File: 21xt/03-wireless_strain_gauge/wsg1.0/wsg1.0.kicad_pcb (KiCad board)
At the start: 2 copper layers, 34 parts, among them J1 GenConn3, J2 GenConn1, J3 GenConn2, U1 ADS1120, U2 102010388

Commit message: First layout 'draft'
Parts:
- removed C1: 22uF, Capacitor_SMD:C_0603_1608Metric
- removed C2: 47uF, Capacitor_SMD:C_0603_1608Metric
- removed R1: 806k, Resistor_SMD:R_0805_2012Metric
- removed R2: 80.6k, Resistor_SMD:R_0603_1608Metric
- added 22u: 22uF, Capacitor_SMD:C_0603_1608Metric, F.Cu at (127.7, 102.7)
- added 47u: 47uF, Capacitor_SMD:C_0603_1608Metric, F.Cu at (125.1, 102.8)
- added 80.6k: 80.6k, Resistor_SMD:R_0603_1608Metric, F.Cu at (124.8, 110.0)
- added 806k: 806k, Resistor_SMD:R_0805_2012Metric, F.Cu at (122.8, 106.4)
- added C13: 0.1uF, Capacitor_SMD:C_0603_1608Metric, F.Cu at (118.3, 120.1)
- added C14: 100uF, Capacitor_SMD:C_0603_1608Metric, F.Cu at (119.9, 120.1)
- TVS1: footprint Diode_THT:D_DO-201AE_P15.24mm_Horizontal -> Diode_SMD:D_0402_1005Metric
- moved J3 58.5 mm to (133.8, 131.0), turned to -90 degrees
- moved R4 57.9 mm to (104.5, 114.3), turned to -90 degrees
- moved R8 57.7 mm to (128.8, 131.3), turned to 90 degrees
- moved J2 55.9 mm to (133.3, 118.6), turned to -90 degrees
- moved C11 55.3 mm to (121.6, 126.1)
- moved C12 54.4 mm to (121.6, 127.6)
- moved J1 53.7 mm to (133.2, 106.5), turned to -90 degrees
- moved R6 53.7 mm to (106.4, 115.5), turned to -90 degrees
- moved U2 53.4 mm to (104.3, 127.8), turned to 90 degrees
- moved R5 53.3 mm to (112.4, 115.5), turned to -90 degrees
- moved C3 52.5 mm to (100.0, 115.0), turned to 180 degrees
- moved C8 51.0 mm to (101.0, 106.6), turned to 90 degrees
- moved C4 48.9 mm to (100.0, 113.4), turned to 180 degrees
- moved R7 46.7 mm to (114.1, 114.1), turned to -90 degrees
- moved C9 44.5 mm to (105.5, 104.2), turned to 90 degrees
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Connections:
- DAC1 pad 2: CS -> CS-DAC
- DAC1 pad 6: DacClr -> unconnected-(DAC1-CLR#-Pad6)
- R7 pad 2: CS -> CS-ADC
- U2 pad 1: DacClr -> CS-DAC
- U2 pad 4: CS -> CS-ADC
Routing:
- net 3v3: track 0.00 -> 52.7 mm
- net CS-ADC: track 0.00 -> 28.8 mm, vias 0 -> 2
- net CS-DAC: track 0.00 -> 27.4 mm, vias 0 -> 1
- net DacLoad: track 0.00 -> 25.1 mm
- net GND: track 0.00 -> 24.3 mm, vias 0 -> 27
- net Ready: track 0.00 -> 22.8 mm
- net GND1: track 0.00 -> 20.4 mm, vias 0 -> 15
- net MOSI: track 0.00 -> 19.6 mm, vias 0 -> 1
- net SClk: track 0.00 -> 15.5 mm
- net Net-(U1-REFP0): track 0.00 -> 12.2 mm
- net 5.5V: track 0.00 -> 11.6 mm, vias 0 -> 10
- net Net-(BConv1-VIN): track 0.00 -> 11.5 mm
- net Net-(LinReg1-VOUT): track 0.00 -> 11.3 mm
- net Net-(InstrAmp1--IN): track 0.00 -> 9.66 mm
- net Net-(InstrAmp1-+IN): track 0.00 -> 9.46 mm
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- added copper zone on In1.Cu, net 5.5V
- added copper zone on F.Cu, net GND
- added copper zone on B.Cu, net GND1
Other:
- board outline added: 47.6 x 40 mm
- copper layers 2 -> 4
- board text added: "0.1u"
- board text added: "100u"
- board text added: "5u"

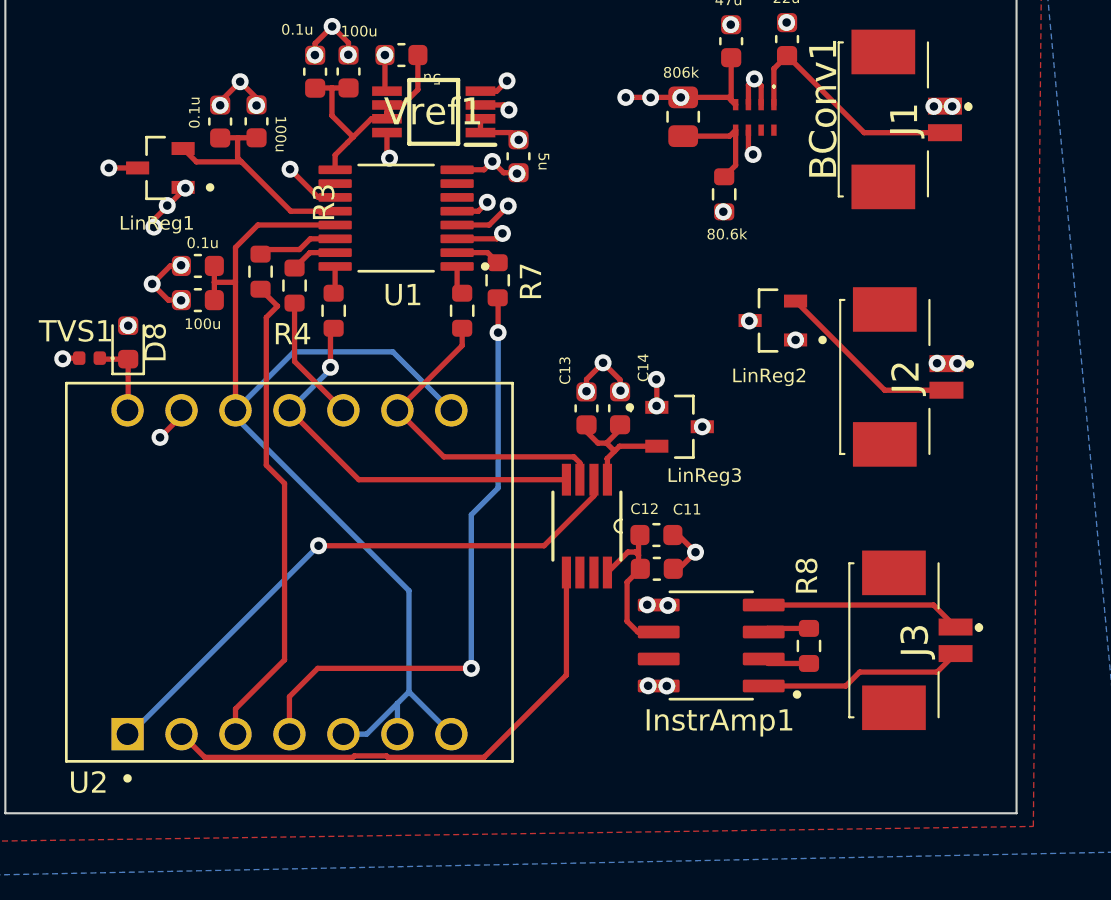
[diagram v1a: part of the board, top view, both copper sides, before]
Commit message: fixed some mistakes in previous layout
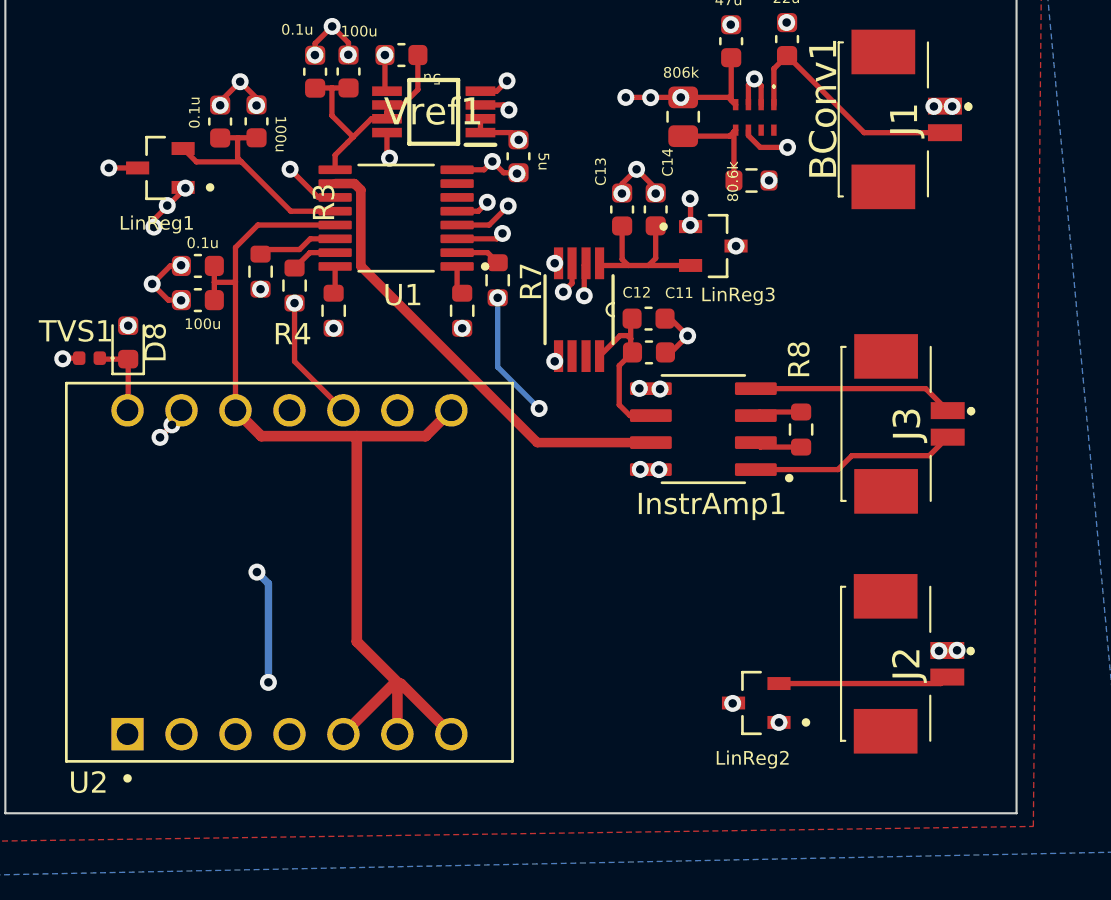
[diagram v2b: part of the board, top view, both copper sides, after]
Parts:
- moved LinReg2 18.0 mm to (126.3, 134.0)
- moved J2 13.5 mm to (133.4, 132.1)
- moved C11 10.2 mm to (121.2, 115.9)
- moved C12 10.2 mm to (121.2, 117.5)
- moved DAC1 10.2 mm to (117.9, 115.5)
- moved InstrAmp1 10.2 mm to (123.8, 121.1)
- moved R8 10.2 mm to (128.4, 121.1)
- moved J3 10.2 mm to (133.4, 120.8)
- moved C13 9.51 mm to (120.0, 110.7)
- moved C14 9.51 mm to (121.5, 110.7)
- moved LinReg3 8.65 mm to (124.2, 112.5)
- moved 80.6k 1.44 mm to (126.0, 109.4), turned to 0 degrees
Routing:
- net AmplifiedSig: track 0.00 -> 22.0 mm
- net MISO: track 6.00 -> 16.7 mm, vias 0 -> 1
- net CS-DAC: track 27.4 -> 32.1 mm
- net 3v3: track 52.7 -> 48.8 mm
- net CS-ADC: track 28.8 -> 26.2 mm
- net Net-(DAC1-VDD): track 6.74 -> 8.31 mm
- net SClk: track 15.5 -> 16.8 mm, vias 0 -> 2
- net GND: track 24.3 -> 25.4 mm
- net MOSI: track 19.6 -> 20.6 mm, vias 1 -> 2
- net Ready: track 22.8 -> 23.7 mm, vias 0 -> 3
- net Net-(J2-Pin_2): track 8.84 -> 8.05 mm
- net GND1: track 20.4 -> 20.0 mm, vias 15 -> 16
- net DacLoad: track 25.1 -> 24.8 mm, vias 0 -> 1

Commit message: hi
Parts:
- added REF**: MountingHole_2.1mm, MountingHole:MountingHole_2.1mm, F.Cu at (145.4, 141.8)
- added REF**: MountingHole_2.1mm, MountingHole:MountingHole_2.1mm, F.Cu at (85.7, 97.5)
- added REF**: MountingHole_2.1mm, MountingHole:MountingHole_2.1mm, F.Cu at (85.0, 141.8)
- added REF**: MountingHole_2.1mm, MountingHole:MountingHole_2.1mm, F.Cu at (144.8, 98.2)
- TVS1: footprint Diode_SMD:D_0402_1005Metric -> Diode_SMD:D_0603_1608Metric
- moved TVS1 0.87 mm to (94.0, 117.8)
- renumbered 22u to C1, 47u to C2, 806k to R1, 80.6k to R2
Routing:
- net 5.5V: track 11.6 -> 13.9 mm, vias 10 -> 12
- net Net-(D8-K): track 3.78 -> 4.33 mm
- net GND: track 25.4 -> 25.9 mm, vias 27 -> 28
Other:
- board size 47.6 x 40 mm -> 67.1 x 51.4 mm

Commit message: hi
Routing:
- net GND: track 25.9 -> 24.7 mm, vias 28 -> 1
- net GND1: track 20.0 -> 20.8 mm

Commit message: hi reid
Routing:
- net GND: track 24.7 -> 29.9 mm, vias 1 -> 28
- net GND1: track 20.8 -> 21.4 mm, vias 16 -> 19

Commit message: oopsie
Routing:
- added copper zone on In2.Cu, net 5.5V
- added copper zone on B.Cu, net GND
- added copper zone on In1.Cu, net GND1
- removed copper zone on In1.Cu, net 5.5V
- removed copper zone on B.Cu, net GND1
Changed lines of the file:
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@@
   (segment (start 116.05 120.1) (end 114.1 118.15) (width 0.25) (layer "B.Cu") (net 33))
   (segment (start 114.1 118.15) (end 114.1 114.89) (width 0.25) (layer "B.Cu") (net 33))
-  (zone (net 2) (net_name "GND") (layer "F.Cu") (hatch edge 0.5)
+  (zone (net 2) (net_name "GND") (layers "F&B.Cu") (hatch edge 0.5)
+    (priority 2)
+    (connect_pads (clearance 0.5))
+    (min_thickness 0.25) (filled_areas_thickness no)
+    (fill yes (thermal_gap 0.5) (thermal_bridge_width 0.5))
+    (polygon
+      (pts
+        (xy 153.88 88.43)
+        (xy 75.17 89.26)
+        (xy 78.32 150.7)
+        (xy 157.7 148.21)
+      )
+    )
+  )
+  (zone (net 8) (net_name "GND1") (layer "In1.Cu") (hatch edge 0.5)
+    (connect_pads (clearance 0.5))
+    (min_thickness 0.25) (filled_areas_thickness no)
+    (fill yes (thermal_gap 0.5) (thermal_bridge_width 0.5))
+    (polygon
+      (pts
+        (xy 79.08 91.14)
+        (xy 80.22 146.63)
+        (xy 151.86 146.14)
+        (xy 150.39 91.96)
+      )
+    )
+  )
+  (zone (net 3) (net_name "5.5V") (layer "In2.Cu") (hatch edge 0.5)
     (priority 1)
     (connect_pads (clearance 0.5))
@@
     (polygon
       (pts
-        (xy 163.66 92.24)
-        (xy 69.28 89.89)
-        (xy 76.57 146.84)
-        (xy 157.11 151.78)
+        (xy 152.02 90.49)
+        (xy 77.45 90.49)
+        (xy 79.73 148.42)
+        (xy 155.13 147.28)
       )
     )
-  )
-  (zone (net 3) (net_name "5.5V") (layer "In1.Cu") (hatch edge 0.5)
-    (connect_pads (clearance 0.5))
-    (min_thickness 0.25) (filled_areas_thickness no)
-    (fill yes (thermal_gap 0.5) (thermal_bridge_width 0.5))
-    (polygon
-      (pts
-        (xy 166.99 88.78)
-        (xy 64.96 86.31)
-        (xy 74.59 148.07)
-        (xy 163.41 155.73)
-      )
-    )
-  )
-  (zone (net 8) (net_name "GND1") (layer "B.Cu") (hatch edge 0.5)
-    (priority 2)
-    (connect_pads (clearance 0.5))
-    (min_thickness 0.25) (filled_areas_thickness no)
-    (fill yes (thermal_gap 0.5) (thermal_bridge_width 0.5))
-    (polygon
-      (pts
-        (xy 169.46 85.69)
-        (xy 62.11 84.45)
-        (xy 68.66 154.37)
-        (xy 165.38 158.57)
-      )
-    )

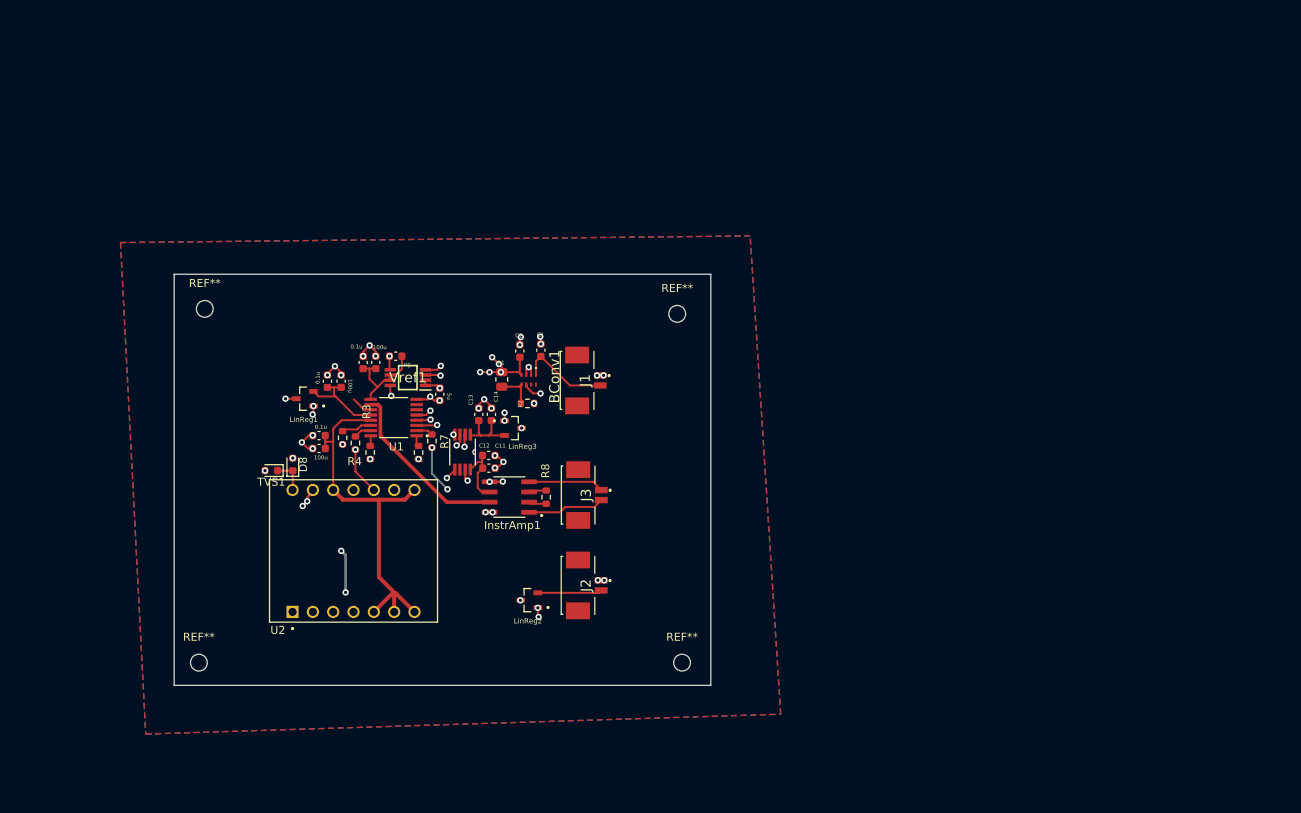
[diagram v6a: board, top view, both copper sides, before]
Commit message: Layout changes to wsg1.0 & Flash memory breakout
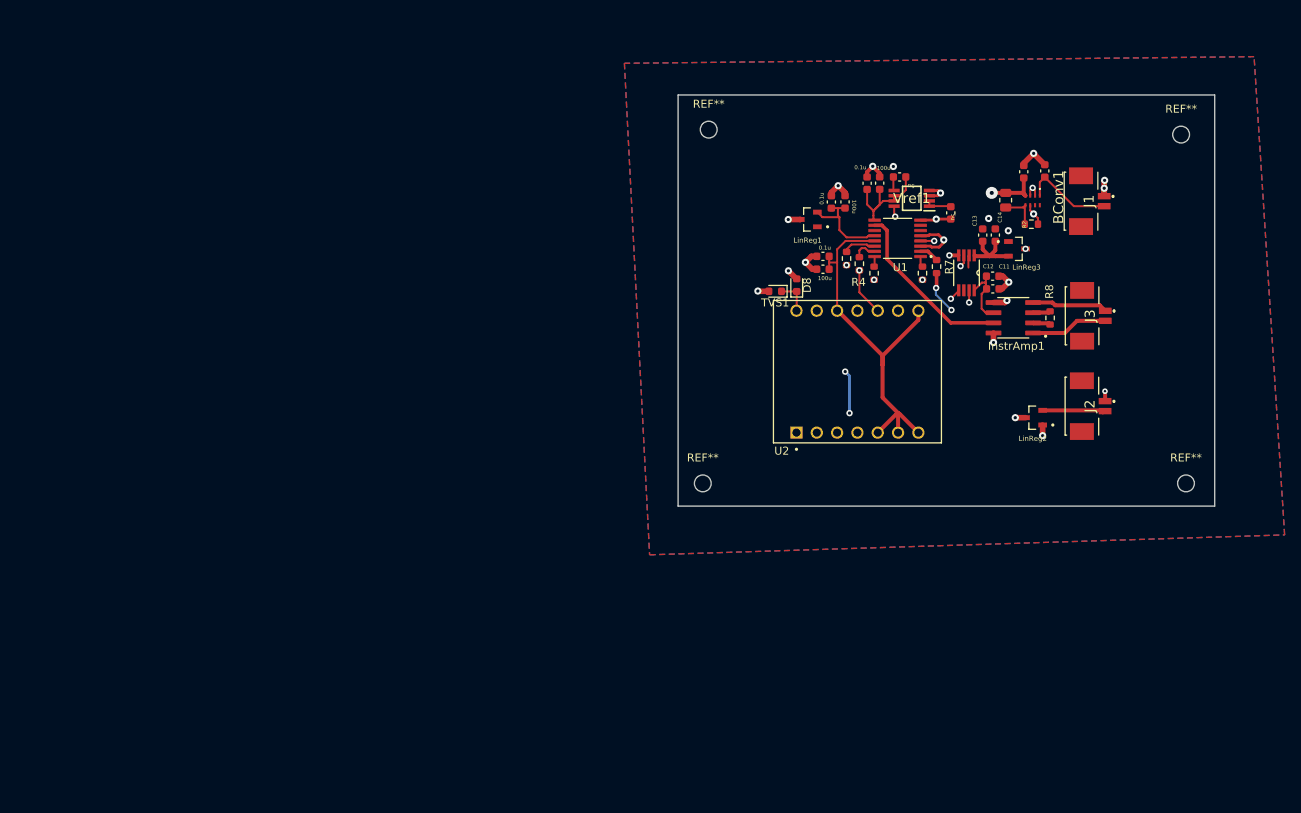
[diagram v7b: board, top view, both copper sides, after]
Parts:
- removed the REF** at (145.4, 141.8)
- removed the REF** at (85.7, 97.5)
- removed the REF** at (85.0, 141.8)
- removed the REF** at (144.8, 98.2)
- added REF**: MountingHole_2.1mm, MountingHole:MountingHole_2.1mm, F.Cu at (208.4, 119.4)
- added REF**: MountingHole_2.1mm, MountingHole:MountingHole_2.1mm, F.Cu at (207.8, 75.8)
- added REF**: MountingHole_2.1mm, MountingHole:MountingHole_2.1mm, F.Cu at (148.7, 75.1)
- added REF**: MountingHole_2.1mm, MountingHole:MountingHole_2.1mm, F.Cu at (148.0, 119.4)
- moved C5 67.8 mm to (179.0, 85.5)
- moved LinReg2 67.1 mm to (189.4, 111.2)
- moved C1 66.9 mm to (190.7, 80.3)
- moved C12 66.9 mm to (184.2, 95.1)
- moved C14 66.9 mm to (184.5, 88.3)
- moved C2 66.9 mm to (188.1, 80.4)
- moved C6 66.9 mm to (172.6, 81.1)
- moved C7 66.9 mm to (165.7, 84.2)
- moved InstrAmp1 66.9 mm to (186.8, 98.7)
- moved J1 66.9 mm to (196.2, 84.1)
- moved J3 66.9 mm to (196.4, 98.4)
- moved LinReg1 66.9 mm to (161.2, 86.4)
- moved LinReg3 66.9 mm to (187.2, 90.0)
- moved R3 66.9 mm to (165.9, 91.3)
- moved R6 66.9 mm to (169.4, 93.1)
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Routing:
- net GND: track 29.9 -> 34.5 mm, vias 28 -> 15
- net GND1: track 21.4 -> 17.2 mm, vias 19 -> 7
- net Net-(U1-REFP0): track 12.2 -> 14.4 mm
- net 5.5V: track 13.9 -> 15.5 mm, vias 12 -> 6
- net Net-(LinReg1-VOUT): track 11.3 -> 12.4 mm
- net 3v3: track 48.5 -> 49.6 mm
- net Net-(U1-DOUT/~DRDY): track 2.21 -> 3.04 mm
- net Net-(DAC1-VDD): track 8.31 -> 8.83 mm
- net CS-DAC: track 32.1 -> 32.2 mm, vias 1 -> 0
